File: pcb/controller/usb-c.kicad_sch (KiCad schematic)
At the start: 11 parts, among them J3 USB_C_Receptacle_USB2.0_16P, U2 CH224K, U4 AMS1117-3.3

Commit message: retraced target pcb
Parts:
- C1, C11: footprint (none) -> Capacitor_SMD:C_1206_3216Metric
- J3: value USB_C_Receptacle_USB2.0_16P -> G-Switch GT-USB-7010ASV; footprint (none) -> Connector_USB:USB_C_Receptacle_G-Switch_GT-USB-7010ASV
- R5: footprint Resistor_SMD:R_0603_1608Metric -> Resistor_SMD:R_1206_3216Metric
- R6, R7, R8: footprint (none) -> Resistor_SMD:R_1206_3216Metric
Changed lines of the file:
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@@
 			)
 		)
-		(property "Footprint" ""
+		(property "Footprint" "Capacitor_SMD:C_1206_3216Metric"
 			(at 69.5452 95.25 0)
 			(effects
@@
 			)
 		)
-		(property "Footprint" ""
+		(property "Footprint" "Resistor_SMD:R_1206_3216Metric"
 			(at 88.9 102.362 90)
 			(effects
@@
 			)
 		)
-		(property "Footprint" ""
+		(property "Footprint" "Resistor_SMD:R_1206_3216Metric"
 			(at 37.592 146.05 90)
 			(effects
@@
 			)
 		)
-		(property "Footprint" "Resistor_SMD:R_0603_1608Metric"
+		(property "Footprint" "Resistor_SMD:R_1206_3216Metric"
 			(at 113.792 119.38 90)
 			(effects
@@
 			)
 		)
-		(property "Value" "USB_C_Receptacle_USB2.0_16P"
+		(property "Value" "G-Switch GT-USB-7010ASV"
 			(at 46.99 99.06 0)
 			(effects
@@
 			)
 		)
-		(property "Footprint" ""
+		(property "Footprint" "Connector_USB:USB_C_Receptacle_G-Switch_GT-USB-7010ASV"
 			(at 50.8 119.38 0)
 			(effects
@@
 			)
 		)
-		(property "Footprint" ""
+		(property "Footprint" "Capacitor_SMD:C_1206_3216Metric"
 			(at 93.6752 95.25 0)
 			(effects
@@
 			)
 		)
-		(property "Footprint" ""
+		(property "Footprint" "Resistor_SMD:R_1206_3216Metric"
 			(at 115.062 104.14 90)
 			(effects

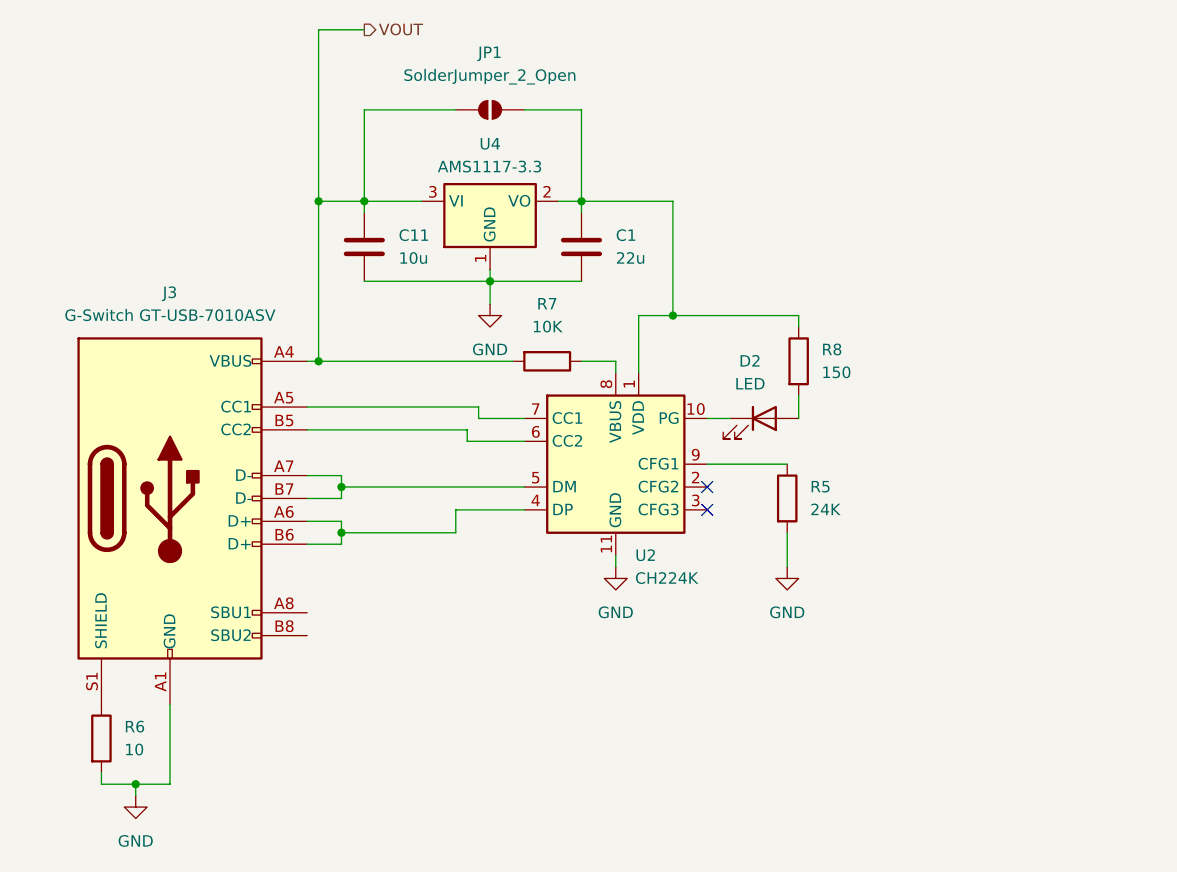
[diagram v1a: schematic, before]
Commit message: added lcsc numbers to all components and added ESD protection
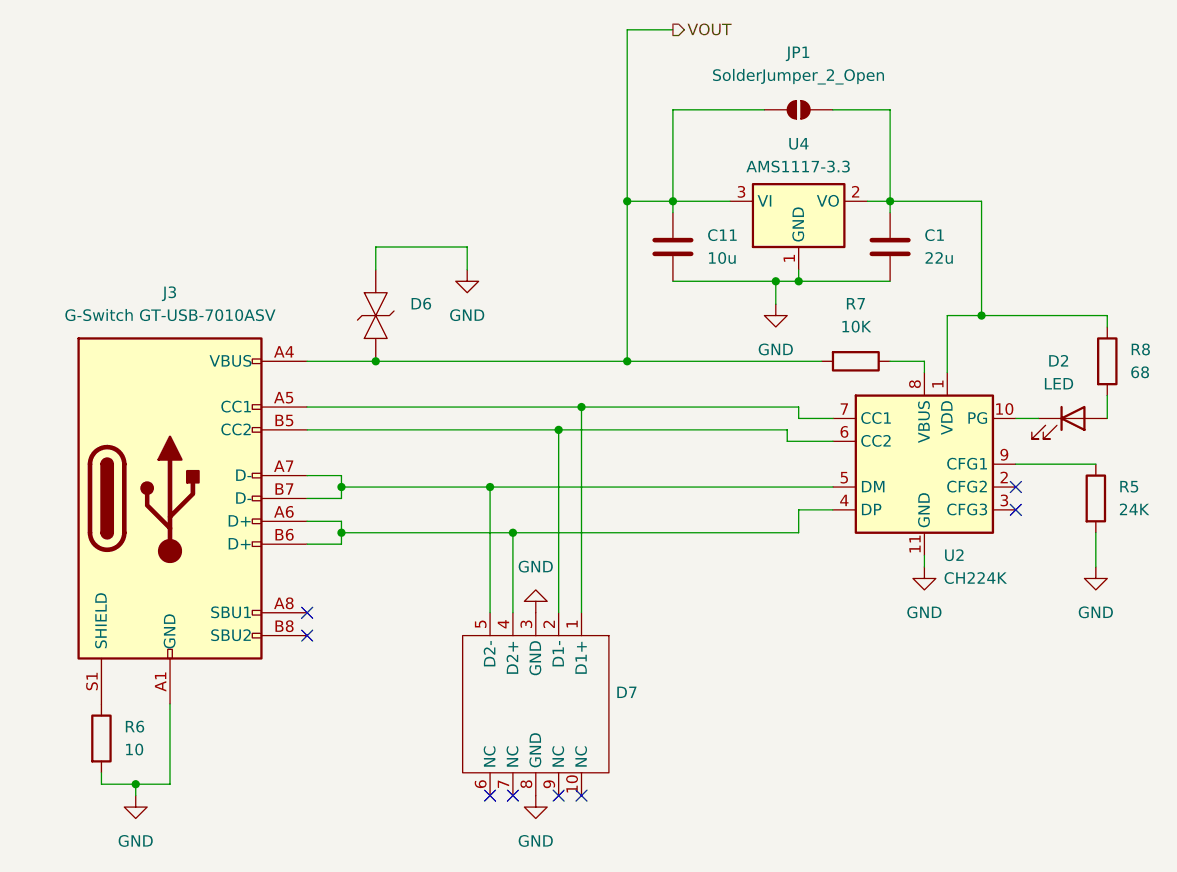
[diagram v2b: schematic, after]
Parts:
- added D6: ~, external_footprints.petty:SMB_L4.4-W3.6-LS5.4-BI, symbol custom:SMBJ24CA_C908853
- added D7: ~, external_footprints.petty:USON-10_L2.5-W1.0-P0.50-BL, symbol custom:TPD4E05U06DQAR_C138714
- C1: footprint Capacitor_SMD:C_1206_3216Metric -> Capacitor_SMD:C_1210_3225Metric; LCSC (none) -> C309062
- C11: footprint Capacitor_SMD:C_1206_3216Metric -> Capacitor_SMD:C_0805_2012Metric; LCSC (none) -> C3039694
- D2: footprint (none) -> LED_SMD:LED_0603_1608Metric; LCSC (none) -> C51933292
- J3: LCSC (none) -> C2988369
- R5: footprint Resistor_SMD:R_1206_3216Metric -> Resistor_SMD:R_0805_2012Metric; LCSC (none) -> C2907246
- R6: footprint Resistor_SMD:R_1206_3216Metric -> Resistor_SMD:R_0805_2012Metric; LCSC (none) -> C17415
- R7: footprint Resistor_SMD:R_1206_3216Metric -> Resistor_SMD:R_0805_2012Metric; LCSC (none) -> C84376
- R8: value 150 -> 68; footprint Resistor_SMD:R_1206_3216Metric -> Resistor_SMD:R_0603_1608Metric; LCSC (none) -> C27592
- U2: LCSC (none) -> C970725
- U4: LCSC (none) -> C347222; now left out of the parts list
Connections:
- net GND: now also D6.2, D7.3 (GND), D7.8 (GND)
- net VOUT: now also D6.1
- net at J3.A6 (D+), J3.B6 (D+), U2.4 (DP): now also D7.4 (D2+)
- net at J3.A7 (D-), J3.B7 (D-), U2.5 (DM): now also D7.5 (D2-)
- net at J3.B5 (CC2), U2.6 (CC2): now also D7.2 (D1-)
- net at J3.A5 (CC1), U2.7 (CC1): now also D7.1 (D1+)
- no-connect marks 2 -> 8
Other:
- moved on the sheet: C1, C11, D2, JP1, R5, R7, R8, U2, U4

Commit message: did led circle pcb and added 3d models for the controller pcb
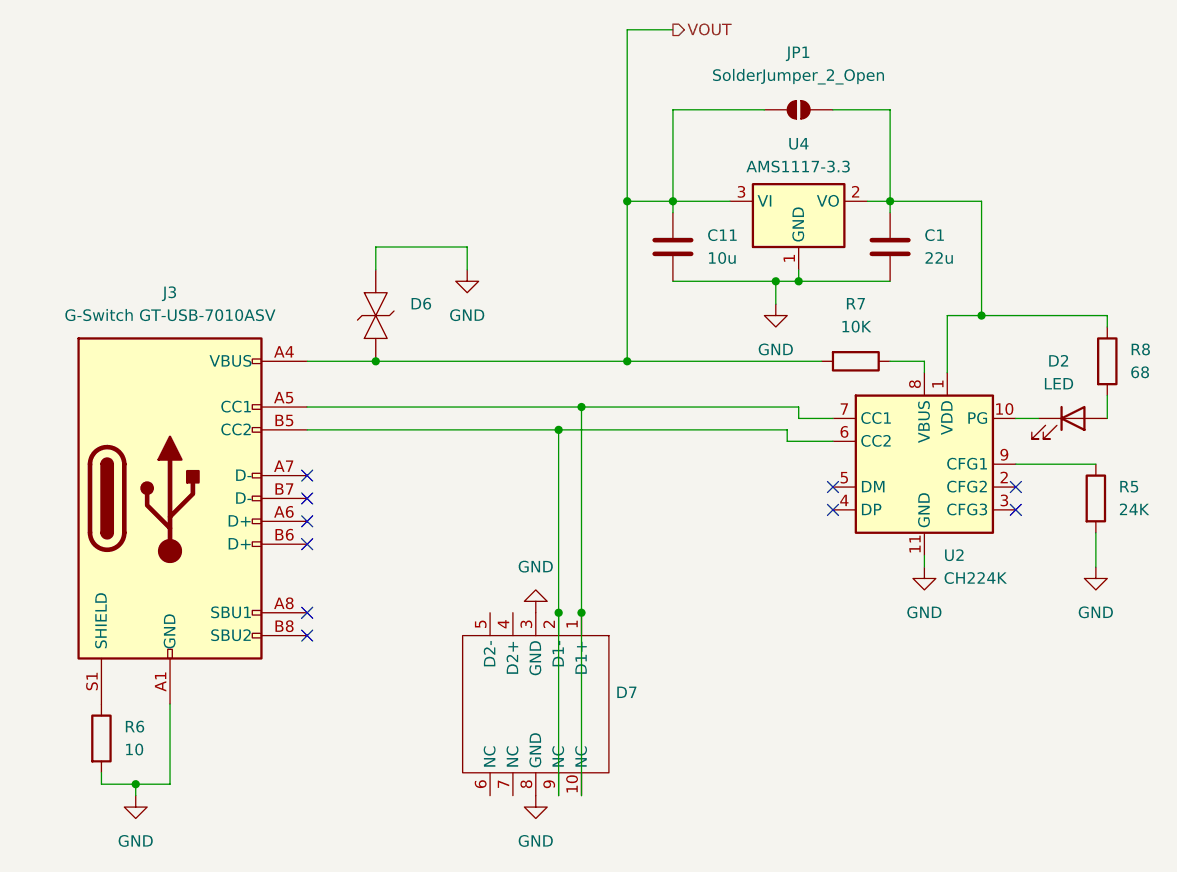
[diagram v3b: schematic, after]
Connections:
- net at D7.2 (D1-), J3.B5 (CC2), U2.6 (CC2): now also D7.9 (NC)
- net at D7.1 (D1+), J3.A5 (CC1), U2.7 (CC1): now also D7.10 (NC)
- now unconnected: D7.4 (D2+), D7.5 (D2-), J3.A6 (D+), J3.A7 (D-), J3.B6 (D+), J3.B7 (D-), U2.4 (DP), U2.5 (DM)
- no-connect marks 8 -> 10
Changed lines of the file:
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@@
 	)
 	(junction
-		(at 82.55 118.11)
+		(at 90.17 132.08)
 		(diameter 0)
 		(color 0 0 0 0)
@@
 	)
 	(junction
-		(at 85.09 123.19)
-		(diameter 0)
-		(color 0 0 0 0)
-	)
-	(junction
-		(at 66.04 118.11)
+		(at 92.71 132.08)
 		(diameter 0)
 		(color 0 0 0 0)
@@
 	)
 	(junction
-		(at 66.04 123.19)
-		(diameter 0)
-		(color 0 0 0 0)
-	)
-	(junction
 		(at 69.85 104.14)
 		(diameter 0)
@@
 	)
 	(no_connect
-		(at 85.09 152.4)
-	)
-	(no_connect
-		(at 82.55 152.4)
-	)
-	(no_connect
-		(at 90.17 152.4)
+		(at 62.23 121.92)
+	)
+	(no_connect
+		(at 120.65 118.11)
+	)
+	(no_connect
+		(at 62.23 119.38)
+	)
+	(no_connect
+		(at 62.23 124.46)
 	)
 	(no_connect
@@
 	)
 	(no_connect
+		(at 62.23 116.84)
+	)
+	(no_connect
 		(at 62.23 134.62)
 	)
 	(no_connect
-		(at 92.71 152.4)
+		(at 120.65 120.65)
 	)
 	(no_connect
@@
 	(wire
 		(pts
-			(xy 116.84 123.19) (xy 116.84 120.65)
-		)
-		(stroke
-			(width 0)
-			(type default)
-		)
-	)
-	(wire
-		(pts
 			(xy 120.65 76.2) (xy 127 76.2)
 		)
@@
 	(wire
 		(pts
-			(xy 66.04 121.92) (xy 66.04 123.19)
-		)
-		(stroke
-			(width 0)
-			(type default)
-		)
-	)
-	(wire
-		(pts
 			(xy 102.87 86.36) (xy 102.87 76.2)
 		)
@@
 	(wire
 		(pts
-			(xy 62.23 119.38) (xy 66.04 119.38)
-		)
-		(stroke
-			(width 0)
-			(type default)
-		)
-	)
-	(wire
-		(pts
-			(xy 66.04 118.11) (xy 66.04 116.84)
-		)
-		(stroke
-			(width 0)
-			(type default)
-		)
-	)
-	(wire
-		(pts
 			(xy 149.86 123.19) (xy 149.86 127)
 		)
@@
 	(wire
 		(pts
-			(xy 85.09 123.19) (xy 116.84 123.19)
-		)
-		(stroke
-			(width 0)
-			(type default)
-		)
-	)
-	(wire
-		(pts
 			(xy 115.57 113.03) (xy 115.57 111.76)
 		)
@@
 	(wire
 		(pts
-			(xy 66.04 116.84) (xy 62.23 116.84)
-		)
-		(stroke
-			(width 0)
-			(type default)
-		)
-	)
-	(wire
-		(pts
-			(xy 82.55 118.11) (xy 120.65 118.11)
-		)
-		(stroke
-			(width 0)
-			(type default)
-		)
-	)
-	(wire
-		(pts
-			(xy 62.23 121.92) (xy 66.04 121.92)
+			(xy 92.71 109.22) (xy 92.71 132.08)
 		)
 		(stroke
@@
 	(wire
 		(pts
-			(xy 66.04 123.19) (xy 85.09 123.19)
-		)
-		(stroke
-			(width 0)
-			(type default)
-		)
-	)
-	(wire
-		(pts
-			(xy 82.55 132.08) (xy 82.55 118.11)
-		)
-		(stroke
-			(width 0)
-			(type default)
-		)
-	)
-	(wire
-		(pts
 			(xy 127 86.36) (xy 137.16 86.36)
 		)
@@
 	(wire
 		(pts
-			(xy 66.04 119.38) (xy 66.04 118.11)
-		)
-		(stroke
-			(width 0)
-			(type default)
-		)
-	)
-	(wire
-		(pts
 			(xy 97.79 86.36) (xy 102.87 86.36)
 		)
@@
 	(wire
 		(pts
-			(xy 116.84 120.65) (xy 120.65 120.65)
-		)
-		(stroke
-			(width 0)
-			(type default)
-		)
-	)
-	(wire
-		(pts
 			(xy 43.18 151.13) (xy 46.99 151.13)
 		)
@@
 	(wire
 		(pts
-			(xy 62.23 124.46) (xy 66.04 124.46)
-		)
-		(stroke
-			(width 0)
-			(type default)
-		)
-	)
-	(wire
-		(pts
-			(xy 66.04 123.19) (xy 66.04 124.46)
+			(xy 90.17 132.08) (xy 90.17 152.4)
 		)
 		(stroke
@@
 	(wire
 		(pts
-			(xy 66.04 118.11) (xy 82.55 118.11)
-		)
-		(stroke
-			(width 0)
-			(type default)
-		)
-	)
-	(wire
-		(pts
 			(xy 62.23 104.14) (xy 69.85 104.14)
 		)
@@
 	(wire
 		(pts
+			(xy 92.71 132.08) (xy 92.71 152.4)
+		)
+		(stroke
+			(width 0)
+			(type default)
+		)
+	)
+	(wire
+		(pts
 			(xy 80.01 93.98) (xy 80.01 91.44)
 		)
 		(stroke
-			(width 0)
-			(type default)
-		)
-	)
-	(wire
-		(pts
-			(xy 85.09 123.19) (xy 85.09 132.08)
-		)
-		(stroke
-			(width 0)
-			(type default)
-		)
-	)
-	(wire
-		(pts
-			(xy 92.71 109.22) (xy 92.71 132.08)
-		)
-		(stroke
